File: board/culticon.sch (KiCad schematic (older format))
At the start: 80 parts, among them J1 Conn_01x02, J2 Conn_01x02, J3 Conn_01x02, J4 Conn_01x02, J5 Conn_01x04, K1 SANYOU_SRD_Form_C, Q1 BT136-500, Q2 BT136-500, Q3 PN2222A, SW1 SW_SPST, SW2 SW_SPST, SW3 SW_SPST, SW4 SW_SPST, T1 Transformer_1P_1S, U1 PC817, U10 RC1602A, U11 DHT11, U12 24LC64, U13 24LC64, U14 DS1307+, U2 PC817, U3 MOC3021M, U4 MOC3021M, U5 L7805, U6 PC817, U7 PC817, U8 ATmega8-16PU, U9 DHT11, Y1 Crystal

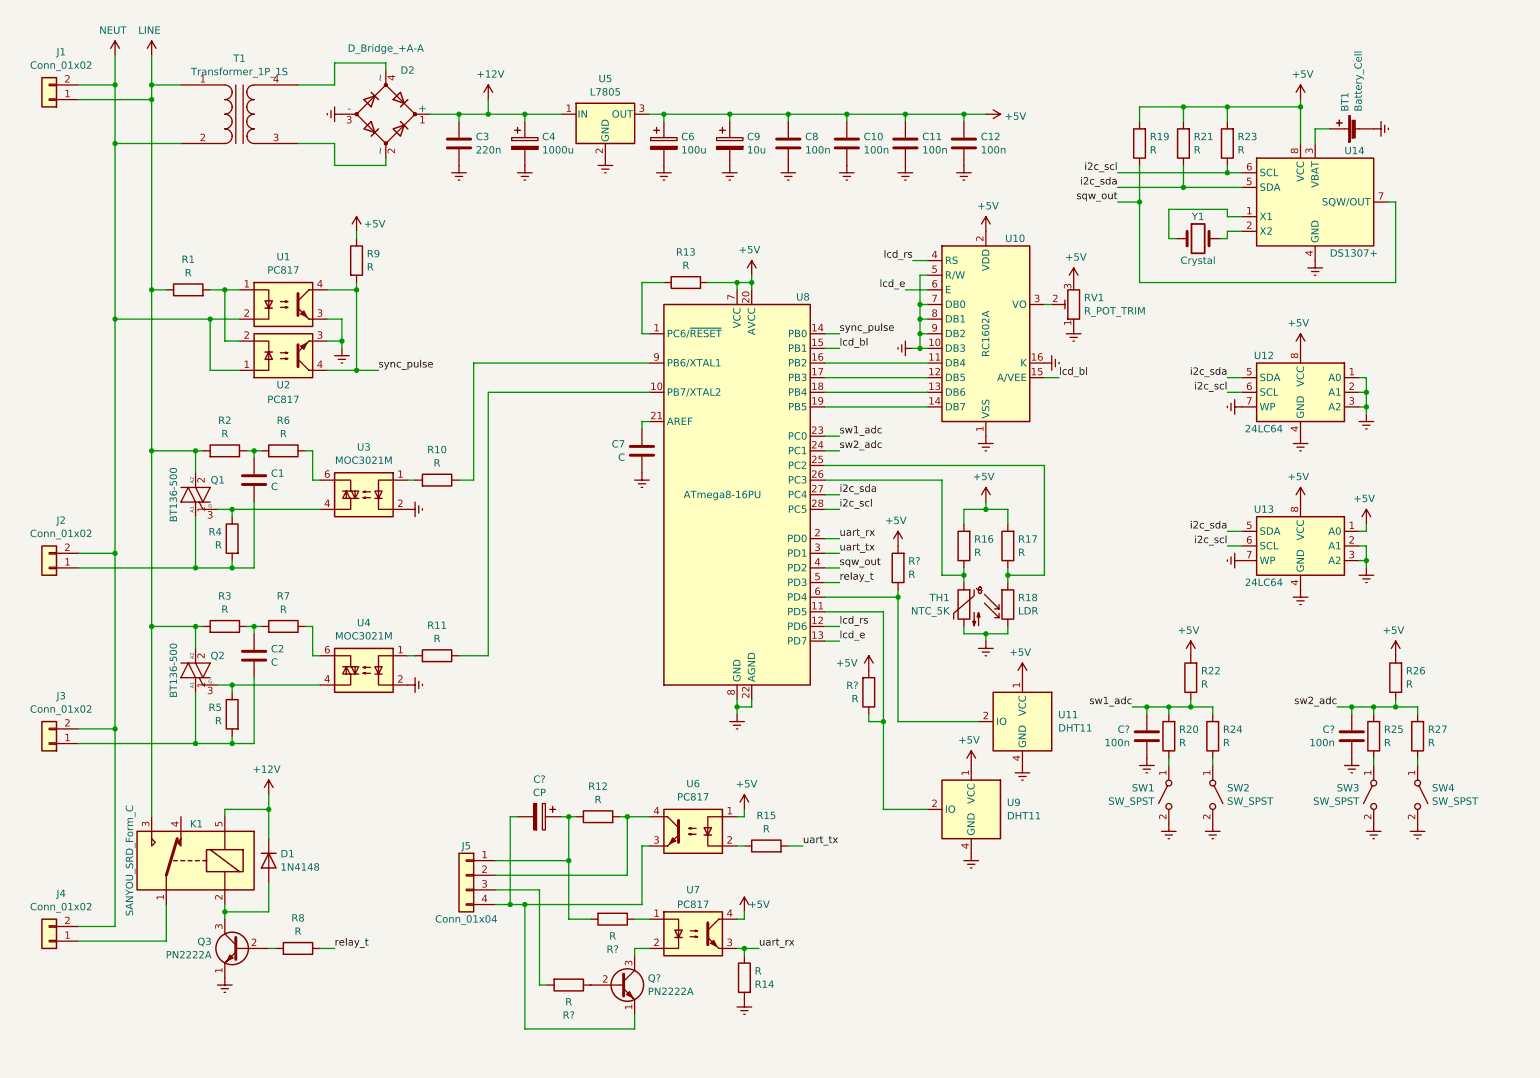
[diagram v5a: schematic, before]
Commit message: schematics additions (sreg & amux)
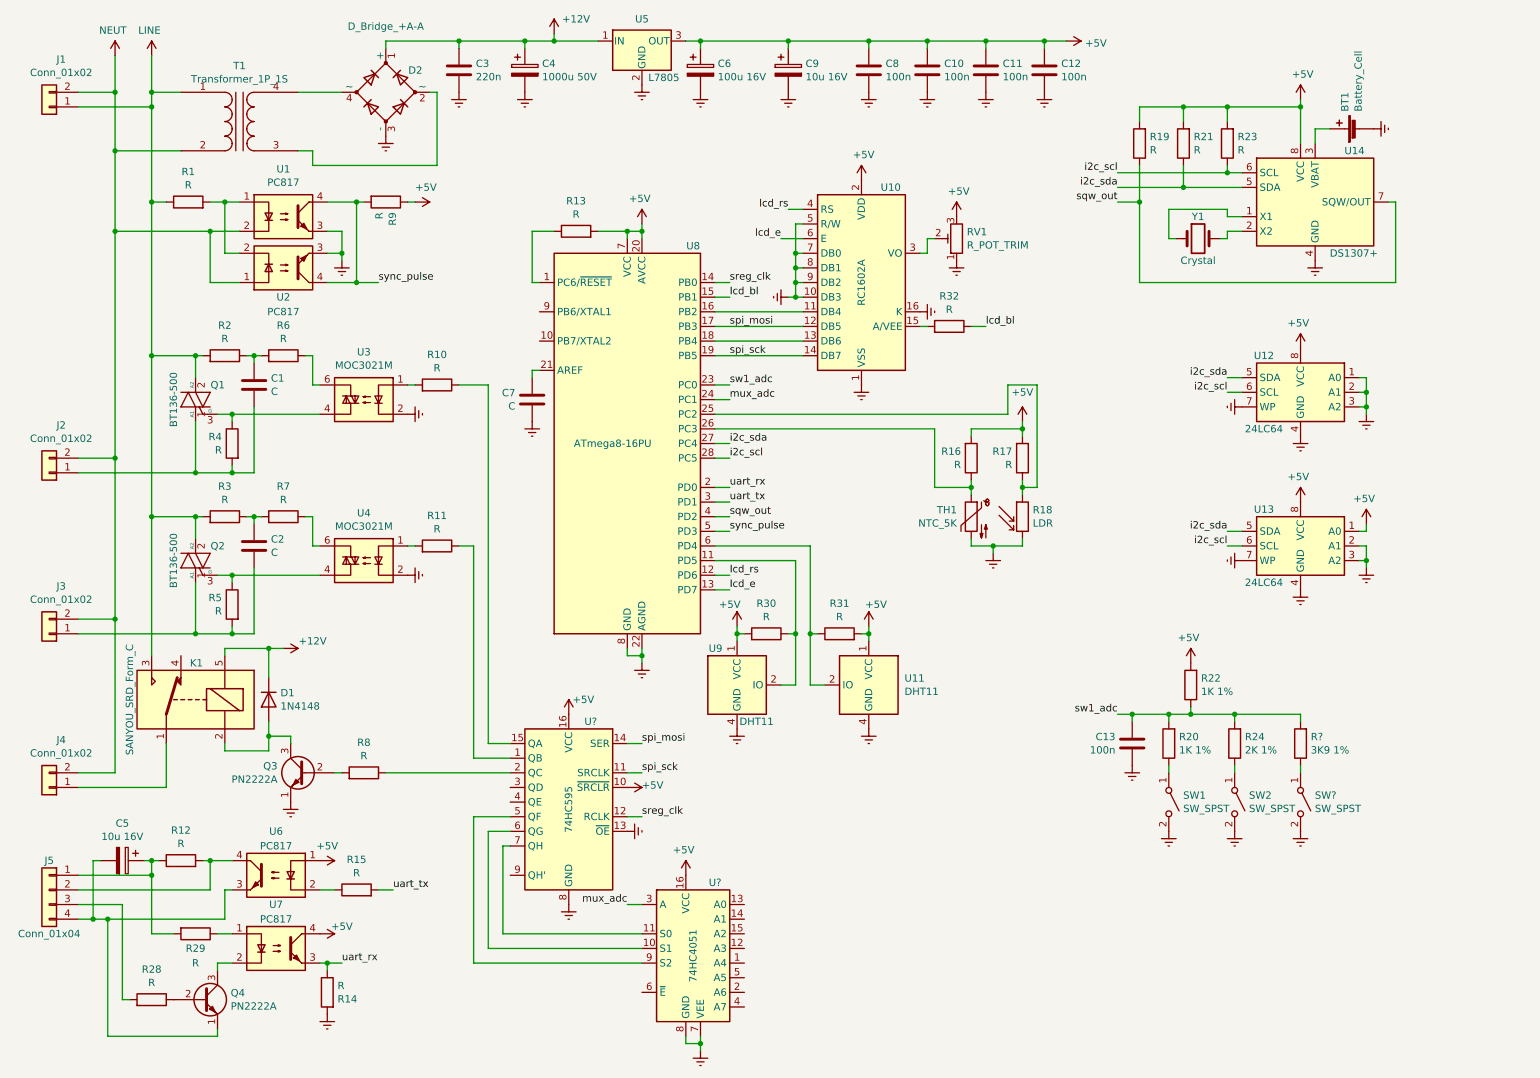
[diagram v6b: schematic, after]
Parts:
- removed C?: 100n, symbol Device:C
- removed R25, R26, R27, R? (x2): R, symbol Device:R
- removed SW3, SW4: SW_SPST, symbol Switch:SW_SPST
- added R30, R31, R32: R, symbol Device:R
- added R?: 3K9 1%, symbol Device:R
- added SW?: SW_SPST, symbol Switch:SW_SPST
- added U?: 74HC595, symbol 74xx:74HC595
- added U?: 74HC4051, symbol 74xx:74HC4051
- C4: value 1000u -> 1000u 50V
- C5: renamed from C?; value CP -> 10u 16V
- C6: value 100u -> 100u 16V
- C9: value 10u -> 10u 16V
- R20, R22: value R -> 1K 1%
- R24: value R -> 2K 1%
- gave numbers to parts that had none: 4
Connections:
- net +5V: now also R30.2, R31.2, U?.10 (~SRCLR), U?.16 (VCC), U?.16 (VCC)
- net Earth: now also SW?.2 (B), U?.13 (~OE), U?.7 (VEE), U?.8 (GND), U?.8 (GND)
- net lcd_bl: now also R32.1; no longer U10.15 (A/VEE)
- net sw1_adc: now also R?.2
- net sync_pulse: now also U8.5 (PD3); no longer U8.14 (PB0)
- net at R10.1: now also U?.15 (QA); no longer U8.9 (PB6/XTAL1)
- net at R11.1: now also U?.1 (QB); no longer U8.10 (PB7/XTAL2)
- net at U8.11 (PD5), U9.2 (IO): now also R30.1
- net at U11.2 (IO), U8.6 (PD4): now also R31.1
- net spi_mosi: now reaches U10.12 (DB5), U8.17 (PB3)
- net spi_mosi: now also U?.14 (SER)
- net spi_sck: now reaches U10.14 (DB7), U8.19 (PB5)
- net spi_sck: now also U?.11 (SRCLK)
- net relay_t: no longer names the net of R8.1
- net relay_t: now also U?.2 (QC); no longer U8.5 (PD3)
- net sw2_adc renamed mux_adc
- net mux_adc: now also U?.3 (A)
- new net: R32.2, U10.15 (A/VEE)
- new net: R?.1, SW?.1 (A)
- new net: U?.5 (QF), U?.9 (S2)
- new net: U?.10 (S1), U?.6 (QG)
- new net: U?.11 (S0), U?.7 (QH)
- new net sreg_clk: U8.14 (PB0), U?.12 (RCLK)
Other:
- moved on the sheet: C1, C10, C11, C12, C13, C2, C3, C4, C5, C6, C7, C8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

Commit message: schem tweaks
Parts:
- removed U9: DHT11, Sensor:Aosong_DHT11_5.5x12.0_P2.54mm, symbol Sensor:DHT11
- added U16: DHT11, Sensor:Aosong_DHT11_5.5x12.0_P2.54mm, symbol Sensor:DHT11
- C7: value C -> 100n
- gave numbers to parts that had none: 4
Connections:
- net +5V: now also U16.1 (VCC)
- net Earth: now also U16.4 (GND)
- net at R30.1, U8.11 (PD5): now also U16.2 (IO)
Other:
- moved on the sheet: BT1, C13, C7, R1, R13, R16, R17, R18, R19, R20, R21, R22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

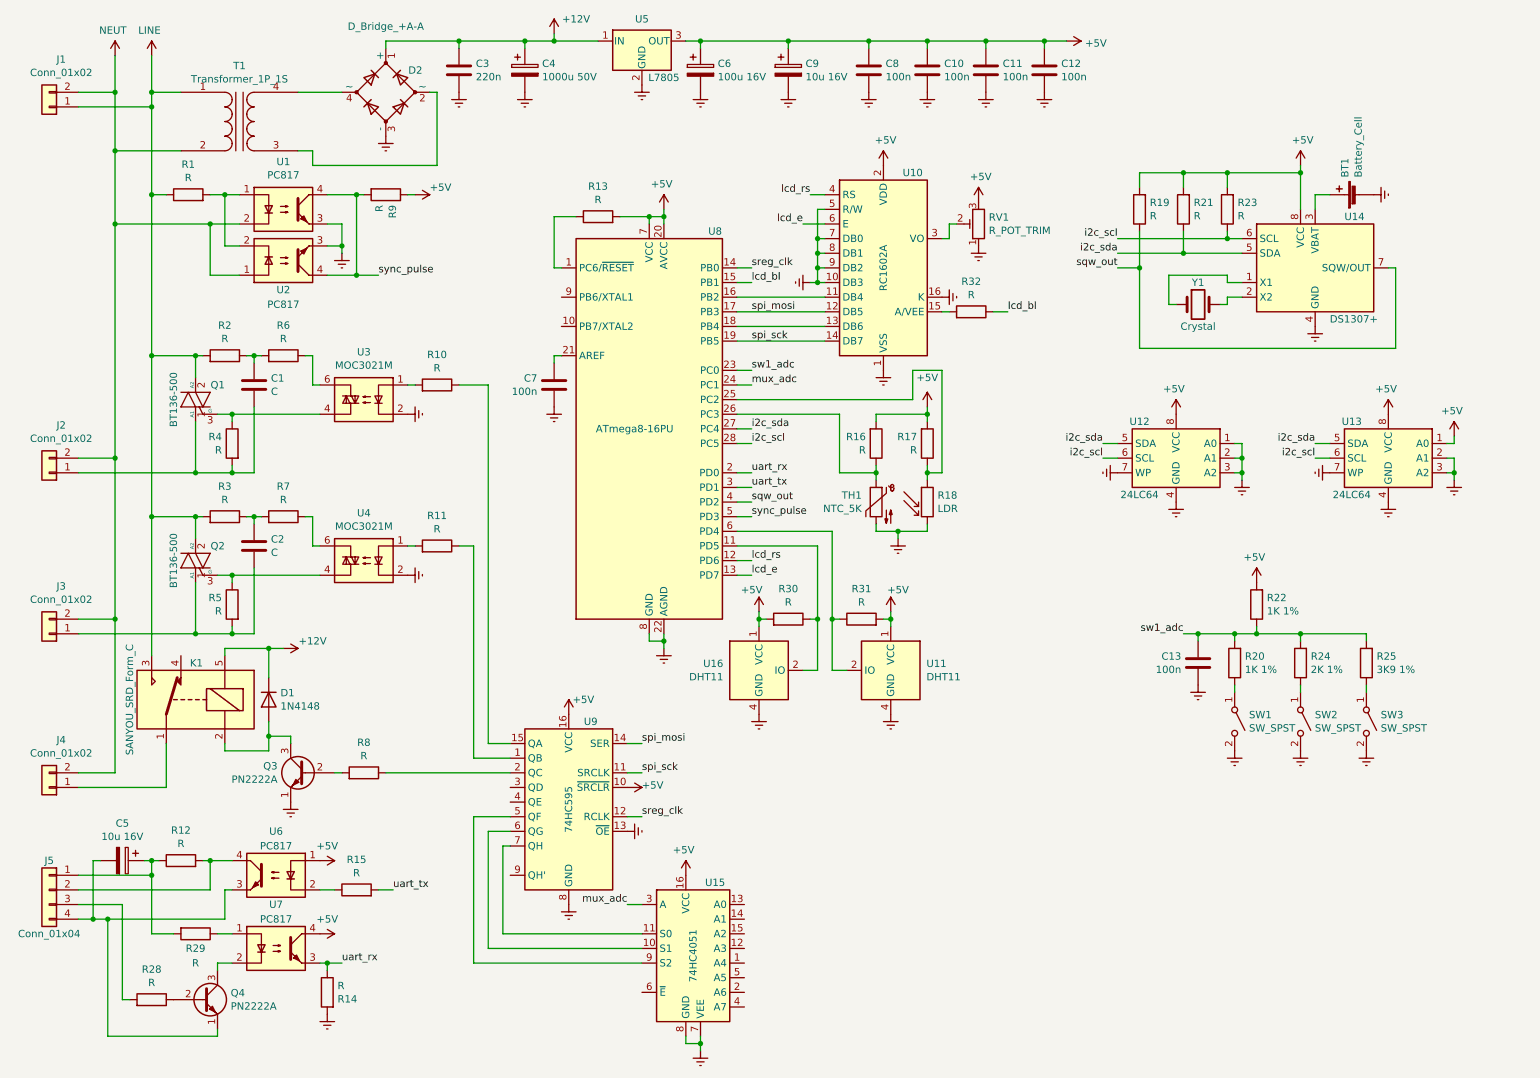
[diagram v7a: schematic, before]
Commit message: sch cosmetic tweaks
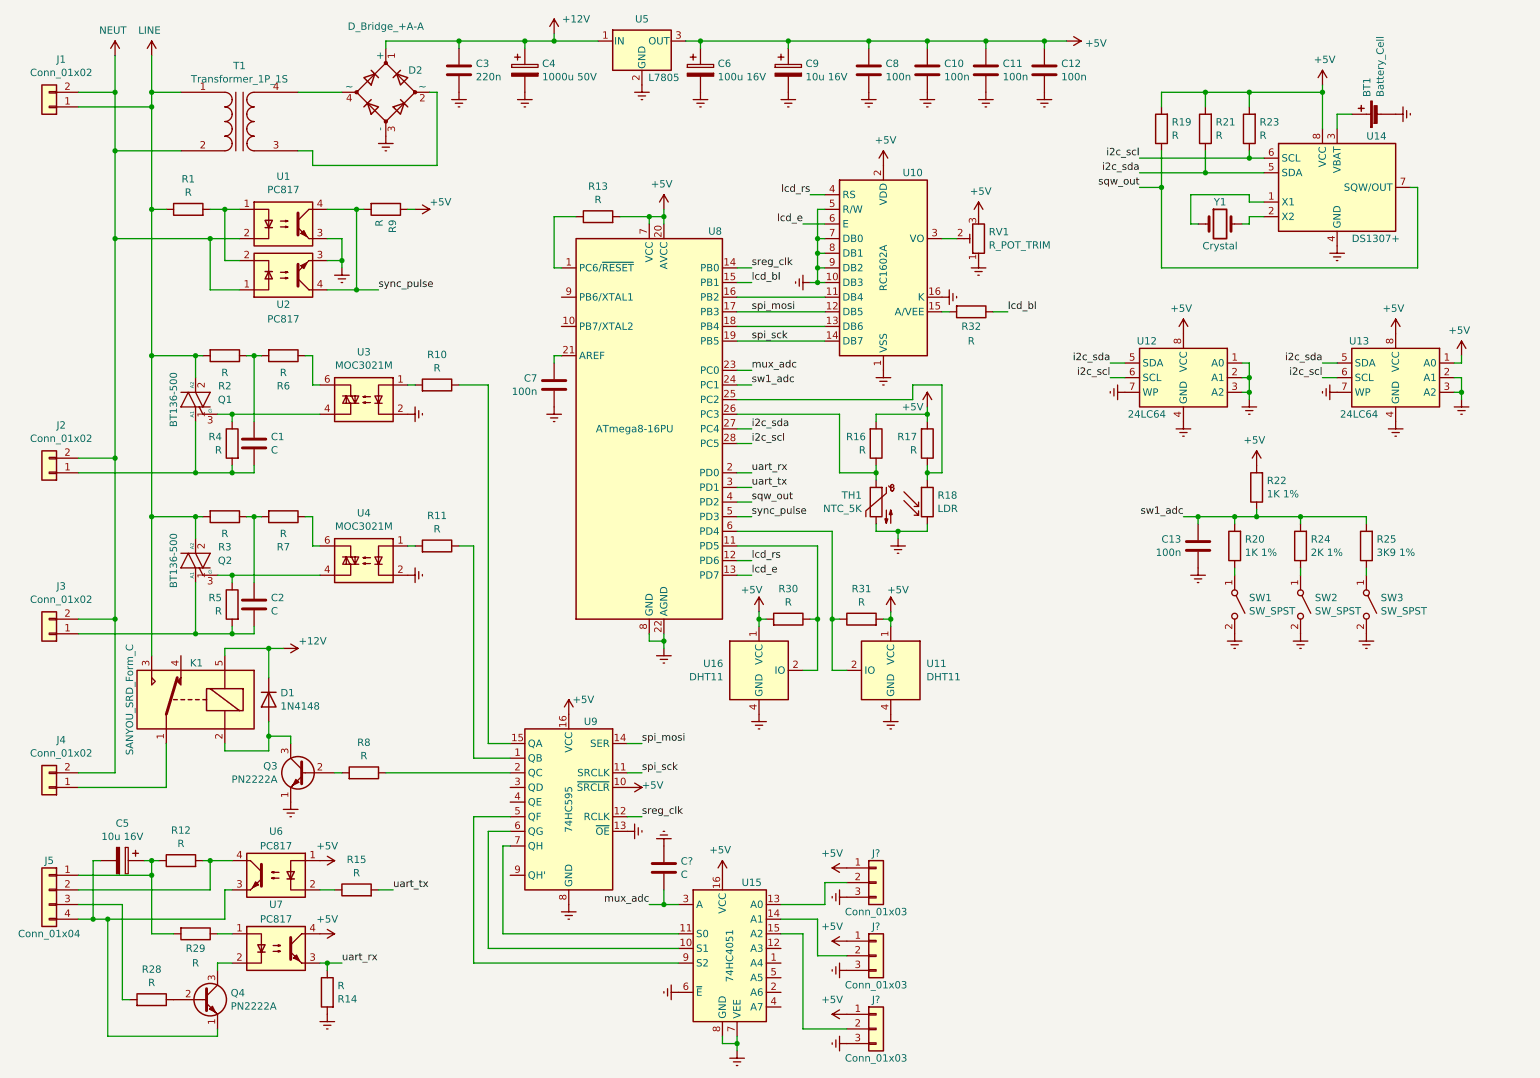
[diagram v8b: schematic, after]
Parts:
- added C?: C, symbol Device:C
- added J? (x3): Conn_01x03, symbol Connector_Generic:Conn_01x03
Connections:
- net +5V: now also J?.1 (Pin_1), J?.1 (Pin_1), J?.1 (Pin_1)
- net Earth: now also U15.6 (~E), C?.2, J?.3 (Pin_3), J?.3 (Pin_3), J?.3 (Pin_3)
- net mux_adc: now also U8.23 (PC0), C?.1; no longer U8.24 (PC1)
- net sw1_adc: now also U8.24 (PC1); no longer U8.23 (PC0)
- net at U15.13 (A0): now also J?.2 (Pin_2)
- net at U15.14 (A1): now also J?.2 (Pin_2)
- net at U15.15 (A2): now also J?.2 (Pin_2)
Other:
- moved on the sheet: BT1, C1, C13, C2, R1, R19, R20, R21, R22, R23, R24, R25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
